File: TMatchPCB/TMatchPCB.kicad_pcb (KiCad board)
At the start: 2 copper layers, 100 x 100 mm, 26 parts, among them J1 CapPlate, J2 CapPlate, J3 BNC, J4 CapPlate, J5 CapPlate, J6 BNC, SW1 SW_SPST, SW2 SW_SPST, SW3 SW_SPST, SW4 SW_SPST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

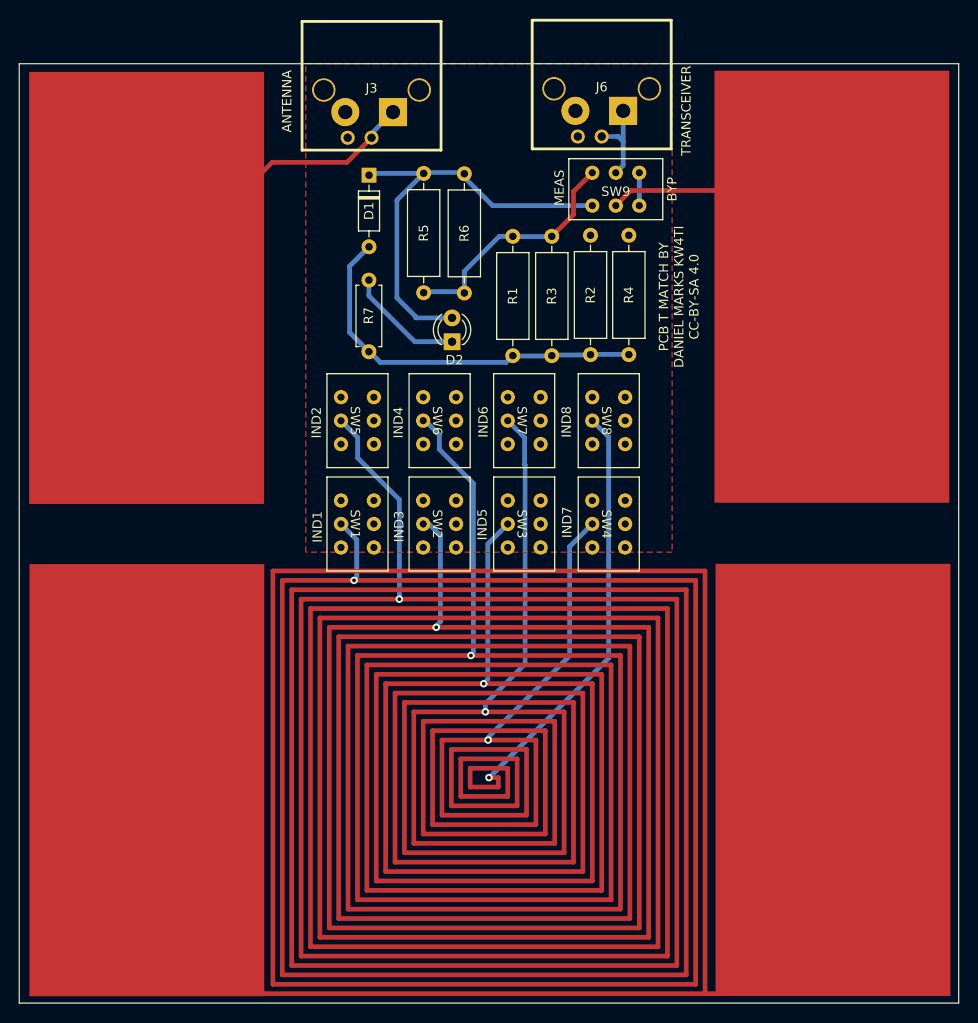
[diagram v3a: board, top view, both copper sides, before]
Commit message: Added 2 more taps for inductor
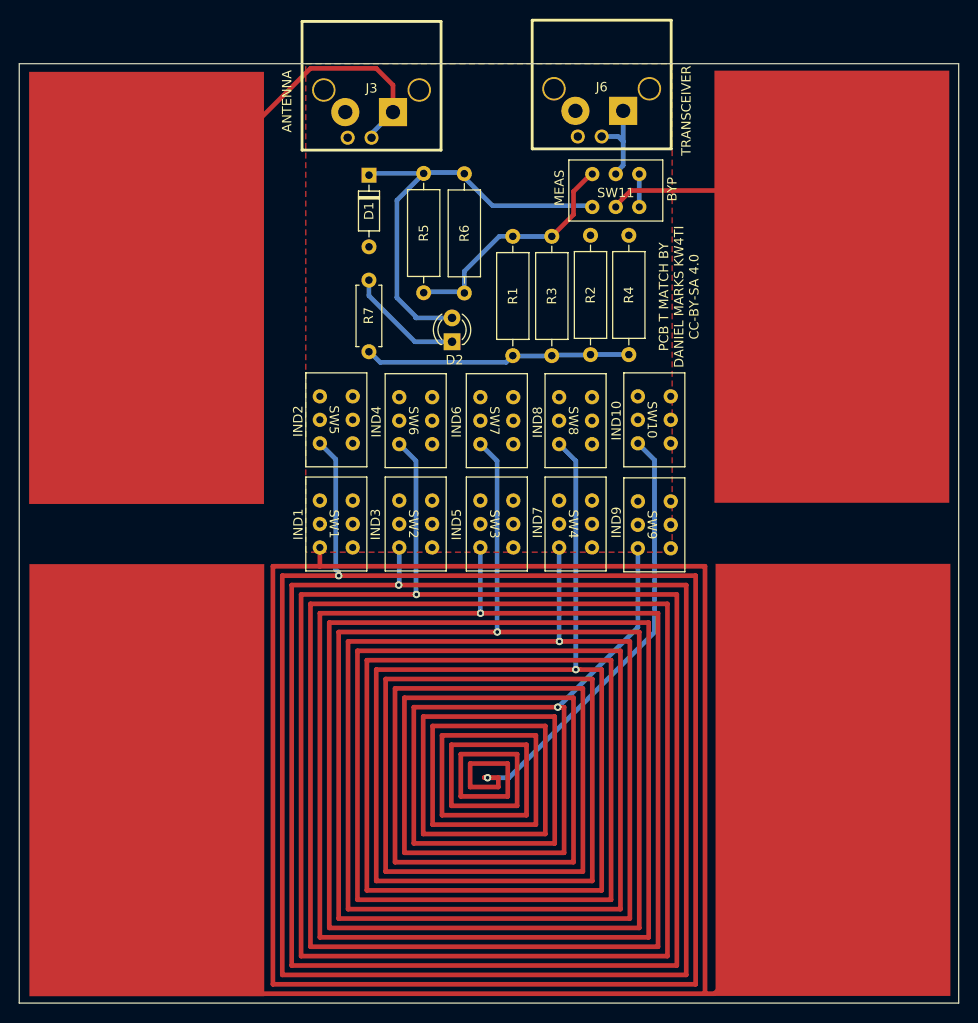
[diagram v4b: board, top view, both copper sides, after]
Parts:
- added SW10: SPST23, TMatchPCB:SS22, F.Cu at (85.9, 57.9)
- added SW11: SW_DPDT_x2, TMatchPCB:SS22, F.Cu at (83.5, 35.2)
- SW1, SW2, SW3, SW4, SW5, SW6, SW7, SW8: value SW_SPST -> SPST23
- SW9: value SW_DPDT_x2 -> SPST23
- moved SW9 34.1 mm to (85.9, 69.1), turned to -90 degrees
- moved SW4 3.53 mm to (77.5, 69.0)
- moved SW8 3.53 mm to (77.5, 58.0)
- moved SW3 2.91 mm to (69.1, 69.0)
- moved SW7 2.91 mm to (69.1, 58.0)
- moved SW2 2.55 mm to (60.5, 69.0)
- moved SW6 2.55 mm to (60.5, 58.0)
- moved SW5 2.25 mm to (52.0, 57.9)
- moved SW1 2.25 mm to (52.0, 69.0)
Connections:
- D2 pad 2: Net-(D2-Pad2) -> Net-(D1-Pad1)
- R1 pad 2: Net-(R1-Pad2) -> Net-(D1-Pad2)
- R2 pad 1: Net-(R1-Pad2) -> Net-(D1-Pad2)
- R3 pad 2: Net-(R1-Pad2) -> Net-(D1-Pad2)
- R4 pad 1: Net-(R1-Pad2) -> Net-(D1-Pad2)
- R5 pad 1: Net-(D2-Pad2) -> Net-(D1-Pad1)
- R6 pad 1: Net-(D2-Pad2) -> Net-(D1-Pad1)
- R7 pad 1: Net-(R1-Pad2) -> Net-(D1-Pad2)
- SW1 pad 1: GND -> (no net)
- SW1 pad 2: Net-(J1-Pad1) -> GND
- SW1 pad 3: (no net) -> Net-(J1-Pad1)
- SW2 pad 1: GND -> (no net)
- SW2 pad 2: Net-(J1-Pad1) -> GND
- SW2 pad 3: (no net) -> Net-(J1-Pad1)
- SW3 pad 1: GND -> (no net)
- SW3 pad 2: Net-(J1-Pad1) -> GND
- SW3 pad 3: (no net) -> Net-(J1-Pad1)
- SW4 pad 1: GND -> (no net)
- SW4 pad 2: Net-(J1-Pad1) -> GND
- SW4 pad 3: (no net) -> Net-(J1-Pad1)
- SW5 pad 1: GND -> (no net)
- SW5 pad 2: Net-(J1-Pad1) -> GND
- SW5 pad 3: (no net) -> Net-(J1-Pad1)
- SW6 pad 1: GND -> (no net)
- SW6 pad 2: Net-(J1-Pad1) -> GND
- SW6 pad 3: (no net) -> Net-(J1-Pad1)
- SW7 pad 1: GND -> (no net)
- SW7 pad 2: Net-(J1-Pad1) -> GND
- SW7 pad 3: (no net) -> Net-(J1-Pad1)
- SW8 pad 1: GND -> (no net)
- SW8 pad 2: Net-(J1-Pad1) -> GND
- SW8 pad 3: (no net) -> Net-(J1-Pad1)
- SW9 pad 1: Net-(D2-Pad2) -> (no net)
- SW9 pad 2: Net-(J5-Pad1) -> GND
- SW9 pad 3: Net-(SW9-Pad3) -> Net-(J1-Pad1)
- SW9 pad 4: Net-(R1-Pad1) -> (no net)
- SW9 pad 5: Net-(J6-Pad1) -> (no net)
- SW9 pad 6: Net-(SW9-Pad3) -> (no net)
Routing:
- net Net-(D2-Pad2): track 47.2 -> 0.00 mm
- net Net-(D1-Pad1): track 0.00 -> 46.8 mm
- net Net-(R1-Pad2): track 41.4 -> 0.00 mm
- net Net-(D1-Pad2): track 0.00 -> 28.5 mm
- net Net-(J1-Pad1): track 2432.6 -> 2407.3 mm, vias 8 -> 9
- net Net-(J3-Pad1): track 40.9 -> 46.7 mm
- net Net-(SW9-Pad3): track 3.50 -> 0.00 mm
- net Net-(SW11-Pad3): track 0.00 -> 3.50 mm
- net Net-(J6-Pad1): track 10.3 -> 9.42 mm
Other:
- board text added: "IND10"
- board text added: "IND9"

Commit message: Tightened up board layout
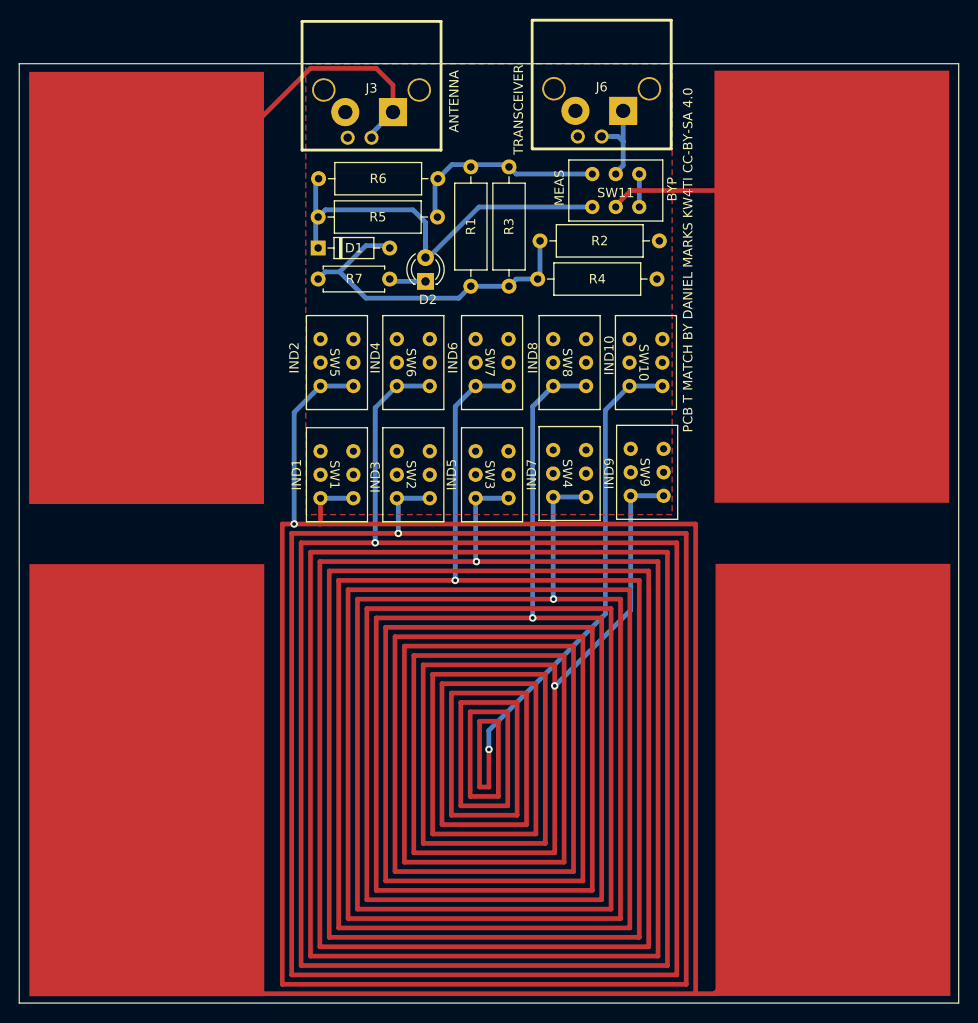
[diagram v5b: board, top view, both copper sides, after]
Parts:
- D1: value 1N5711 -> 1N4148
- SW1, SW10, SW2, SW3, SW4, SW5, SW6, SW7, SW8, SW9: footprint TMatchPCB:SS22 -> TMatchPCB:SS22NB
- moved R6 15.5 mm to (51.9, 32.2), turned to 0 degrees
- moved R2 13.2 mm to (75.4, 38.9), turned to 0 degrees
- moved R4 12.6 mm to (75.2, 42.9), turned to 0 degrees
- moved R5 12.2 mm to (51.8, 36.3), turned to 0 degrees
- moved D1 9.46 mm to (51.8, 39.6), turned to 0 degrees
- moved R7 9.43 mm to (51.8, 42.9), turned to 0 degrees
- moved R3 8.68 mm to (72.1, 31.0)
- moved R1 8.64 mm to (68.1, 31.0)
- moved D2 7.01 mm to (63.2, 43.2)
- moved SW8 6.22 mm to (76.8, 51.8)
- moved SW7 6.20 mm to (68.6, 51.8)
- moved SW6 6.19 mm to (60.2, 51.8)
- moved SW10 6.16 mm to (85.0, 51.8)
- moved SW5 6.10 mm to (52.1, 51.8)
- moved SW9 5.64 mm to (85.1, 63.5)
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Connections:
- R1 pad 2: Net-(D1-Pad2) -> Net-(R1-Pad2)
- R2 pad 1: Net-(D1-Pad2) -> Net-(R1-Pad2)
- R3 pad 2: Net-(D1-Pad2) -> Net-(R1-Pad2)
- R4 pad 1: Net-(D1-Pad2) -> Net-(R1-Pad2)
- R7 pad 1: Net-(D1-Pad2) -> Net-(R1-Pad2)
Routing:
- net Net-(J1-Pad1): track 2407.3 -> 2561.1 mm
- net Net-(R1-Pad2): track 0.00 -> 36.4 mm
- net Net-(D1-Pad2): track 28.5 -> 0.00 mm
- net Net-(D2-Pad1): track 12.5 -> 3.92 mm
- net Net-(R1-Pad1): track 26.2 -> 22.0 mm
- net Net-(D2-Pad2): track 46.8 -> 43.9 mm

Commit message: Picture of assembled T Match
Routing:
- net Net-(J1-Pad1): track 2561.1 -> 2562.1 mm
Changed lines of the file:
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@@
   (segment (start 57.89 71) (end 50 71) (width 0.5) (layer "F.Cu") (net 10))
   (segment (start 52 69) (end 52.07 68.93) (width 0.5) (layer "F.Cu") (net 10))
-  (segment (start 81 80) (end 59 80) (width 0.5) (layer "F.Cu") (net 10))
   (segment (start 65 101) (end 74 101) (width 0.5) (layer "F.Cu") (net 10))
   (segment (start 106.62 106.38) (end 106.62 96.24) (width 0.5) (layer "F.Cu") (net 10))
@@
   (segment (start 76.87 77) (end 56 77) (width 0.5) (layer "F.Cu") (net 10))
   (segment (start 52.07 68.93) (end 52.07 66.254) (width 0.5) (layer "F.Cu") (net 10))
+  (segment (start 74.64 80) (end 59 80) (width 0.5) (layer "F.Cu") (net 10))
   (segment (start 69 97) (end 70 97) (width 0.5) (layer "F.Cu") (net 10))
   (segment (start 60.35 70) (end 49 70) (width 0.5) (layer "F.Cu") (net 10))
@@
   (segment (start 49.26 69) (end 48 69) (width 0.5) (layer "F.Cu") (net 10))
   (segment (start 51 115) (end 88 115) (width 0.5) (layer "F.Cu") (net 10))
+  (segment (start 81 80) (end 74.64 80) (width 0.5) (layer "F.Cu") (net 10))
   (segment (start 78 83) (end 62 83) (width 0.5) (layer "F.Cu") (net 10))
   (segment (start 69 90) (end 69 97) (width 0.5) (layer "F.Cu") (net 10))
@@
   (via (at 49.26 69) (size 0.8) (drill 0.4) (layers "F.Cu" "B.Cu") (net 10))
   (via (at 66.41 75) (size 0.8) (drill 0.4) (layers "F.Cu" "B.Cu") (net 10))
-  (via (at 74.65 79) (size 0.8) (drill 0.4) (layers "F.Cu" "B.Cu") (net 10))
+  (via (at 74.64 80) (size 0.8) (drill 0.4) (layers "F.Cu" "B.Cu") (net 10))
   (via (at 68.67 73) (size 0.8) (drill 0.4) (layers "F.Cu" "B.Cu") (net 10))
   (via (at 57.89 71) (size 0.8) (drill 0.4) (layers "F.Cu" "B.Cu") (net 10))
@@
   (segment (start 82.4 78.57) (end 82.4 56.879) (width 0.5) (layer "B.Cu") (net 10))
   (segment (start 76.87 77) (end 76.835 76.965) (width 0.5) (layer "B.Cu") (net 10))
+  (segment (start 76.835 54.316) (end 74.65 56.501) (width 0.5) (layer "B.Cu") (net 10))
   (segment (start 68.67 73) (end 68.58 72.91) (width 0.5) (layer "B.Cu") (net 10))
   (segment (start 57.89 71) (end 57.89 56.624) (width 0.5) (layer "B.Cu") (net 10))
   (segment (start 72.588 66.254) (end 69.088 66.254) (width 0.5) (layer "B.Cu") (net 10))
-  (segment (start 74.65 56.501) (end 76.835 54.316) (width 0.5) (layer "B.Cu") (net 10))
-  (segment (start 74.65 79) (end 74.65 56.501) (width 0.5) (layer "B.Cu") (net 10))
+  (segment (start 74.65 79.99) (end 74.64 80) (width 0.5) (layer "B.Cu") (net 10))
   (segment (start 57.89 56.624) (end 60.198 54.316) (width 0.5) (layer "B.Cu") (net 10))
   (segment (start 80.335 54.316) (end 76.835 54.316) (width 0.5) (layer "B.Cu") (net 10))
@@
   (segment (start 88.59 66) (end 85.09 66) (width 0.5) (layer "B.Cu") (net 10))
   (segment (start 80.335 66.127) (end 76.835 66.127) (width 0.5) (layer "B.Cu") (net 10))
+  (segment (start 74.65 56.501) (end 74.65 79.99) (width 0.5) (layer "B.Cu") (net 10))
   (segment (start 55.57 54.316) (end 52.07 54.316) (width 0.5) (layer "B.Cu") (net 10))
   (segment (start 66.41 75) (end 66.41 56.486) (width 0.5) (layer "B.Cu") (net 10))

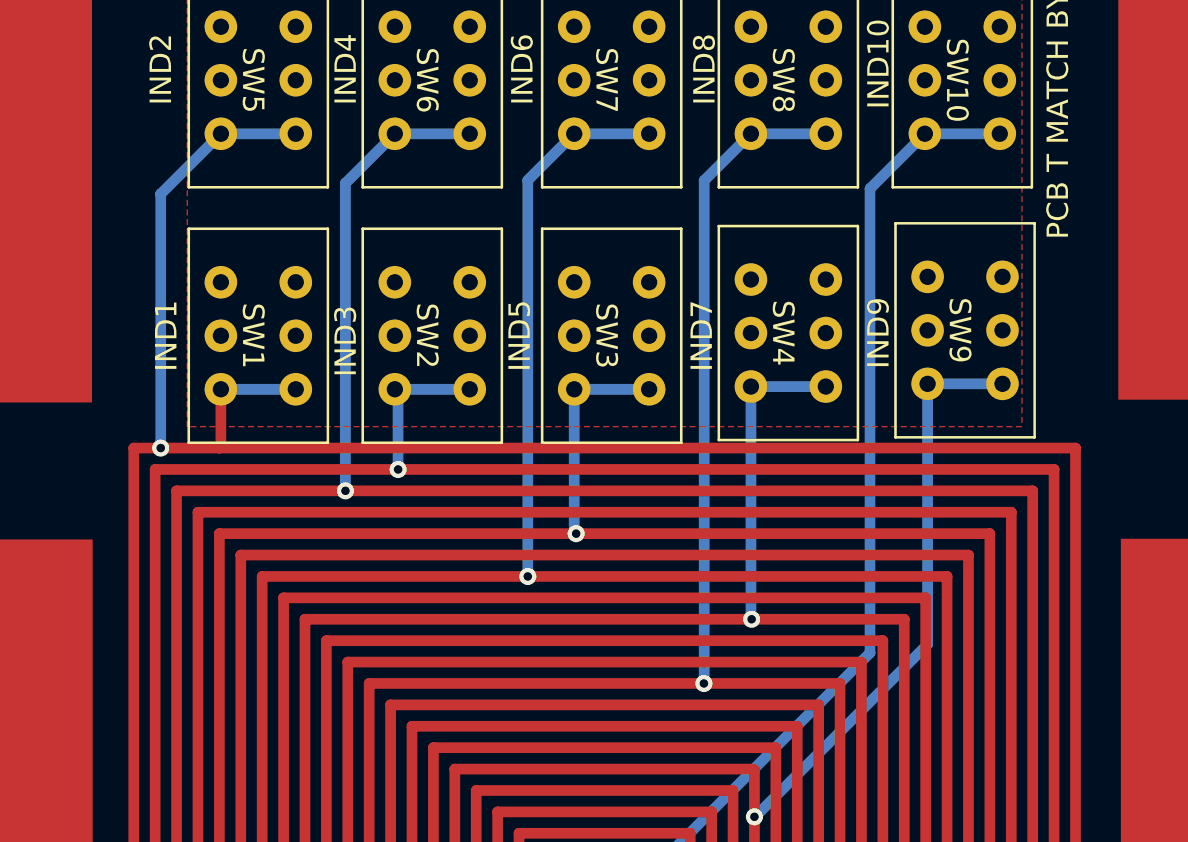
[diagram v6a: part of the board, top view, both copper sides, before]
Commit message: Fixed taps
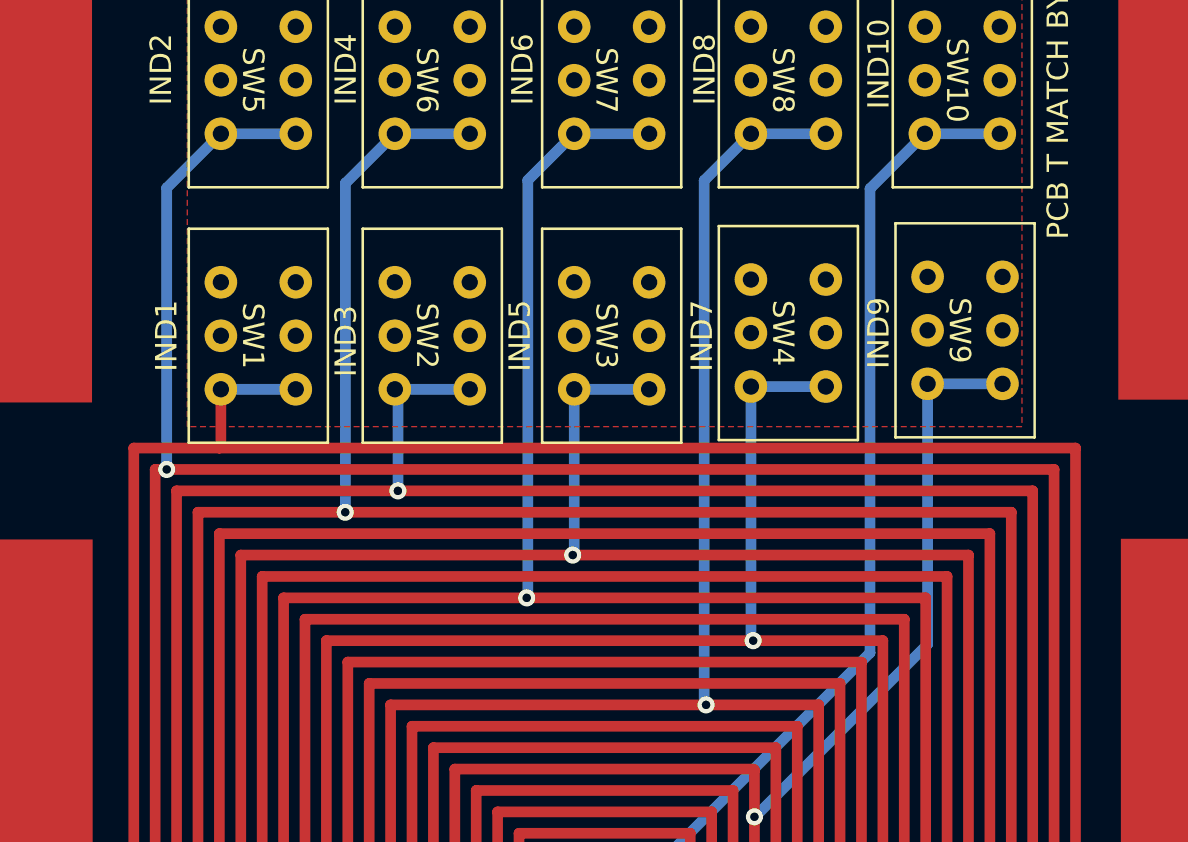
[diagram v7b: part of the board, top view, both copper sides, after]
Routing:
- net Net-(J1-Pad1): track 2562.1 -> 2569.1 mm

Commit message: Added silkscreen instructions and one slide plate
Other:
- board text added: "ANTENNA SIDE"
- board text added: "OFF"
- board text added: "ON"
- board text added: "TRANSMITTER SIDE"
- board text added: "The rough guide to tuning a T-match. - Switch the tuner bridge from BYP to MEAS. - Set the transmitter for low power (less than 5 W) in case the transmitter is capable than more than this power. - Set the capacitor plates on the antenna side for maximum overlap and those on the transmit side for half overlap. - Switching ON only one inductor switch at a time, find the position which dims the LED 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"
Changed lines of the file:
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@@
     (property "Sheetname" "")
     (attr through_hole)
-    (fp_text reference "D2" (at -1.945 0.26) (layer "F.SilkS")
+    (fp_text reference "D2" (at 4.31 -0.036) (layer "F.SilkS")
       (effects (font (size 1 1) (thickness 0.15)))
     )
@@
     (effects (font (size 1 1) (thickness 0.15)) (justify mirror))
   )
+  (gr_text "The rough guide to tuning a T-match.\n\n- Switch the tuner bridge from BYP to MEAS. \n- Set the transmitter for low power (less than 5 W)\n  in case the transmitter is capable than more than\n  this power.\n- Set the capacitor plates on the antenna side for \n  maximum overlap and those on the transmit side\n  for half overlap.\n- Switching ON only one inductor switch at a time,\n  find the position which dims the LED the most.\n- Slide and retighten the capacitor on the transmitter\n  side to dim the LED.\n- Test the other inductor settings to see if the LED\n  can be further dimmed (antenna better matched).\n- Alternate between the transmitter capacitor and \n  inductor to minimize the LED brightness.\n- After tuning the input capacitor and inductor switch,\n  adjust the antenna side capacitor for minimum \n  brightness.  Once you have done this, repeat \n  returning the transmit side capacitor and inductor.\n  The goal is to maximize the antenna side capacitance\n  while achieving a good match with the transmit side\n  capacitor and inductor tap.\n- Record which inductor tap is switched and the \n  position of the plates as indicated by the ruled \n  line position on the edge of the tuner plate for \n  the transmit and antenna side capacitors.\n- Switch the tuner bridge from MEAS to BYP before\n  transmitting.\n" (at 91.5 95) (layer "B.SilkS")
+    (effects (font (size 1 1) (thickness 0.15)) (justify left mirror))
+  )
   (gr_text "4" (at 29 119) (layer "B.SilkS")
     (effects (font (size 1 1) (thickness 0.15)) (justify mirror))
@@
     (effects (font (size 1 1) (thickness 0.15)) (justify mirror))
   )
+  (gr_text "ANTENNA SIDE" (at 48.5 82.5 -90) (layer "B.SilkS")
+    (effects (font (size 1 1) (thickness 0.15)) (justify mirror))
+  )
   (gr_text "10" (at 41 119) (layer "B.SilkS")
     (effects (font (size 1 1) (thickness 0.15)) (justify mirror))
@@
     (effects (font (size 1 1) (thickness 0.15)) (justify mirror))
   )
+  (gr_text "TRANSMITTER SIDE" (at 92.5 83.5 -90) (layer "B.SilkS")
+    (effects (font (size 1 1) (thickness 0.15)) (justify mirror))
+  )
   (gr_text "7" (at 105 21) (layer "B.SilkS")
     (effects (font (size 1 1) (thickness 0.15)) (justify mirror))
@@
     (effects (font (size 1 1) (thickness 0.15)))
   )
+  (gr_text "ON" (at 70.33 69.5) (layer "F.SilkS")
+    (effects (font (size 1 1) (thickness 0.15)))
+  )
   (gr_text "BYP" (at 89.5 33.36 90) (layer "F.SilkS")
     (effects (font (size 1 1) (thickness 0.15)))
@@
     (effects (font (size 1 1) (thickness 0.15)))
   )
+  (gr_text "ON" (at 61.948 69.5) (layer "F.SilkS")
+    (effects (font (size 1 1) (thickness 0.15)))
+  )
   (gr_text "IND2" (at 49.276 51.308 90) (layer "F.SilkS")
     (effects (font (size 1 1) (thickness 0.15)))
   )
+  (gr_text "ON" (at 87 69.5) (layer "F.SilkS")
+    (effects (font (size 1 1) (thickness 0.15)))
+  )
   (gr_text "IND5" (at 66.04 63.754 90) (layer "F.SilkS")
     (effects (font (size 1 1) (thickness 0.15)))
   )
+  (gr_text "ON" (at 53.82 69.5) (layer "F.SilkS")
+    (effects (font (size 1 1) (thickness 0.15)))
+  )
   (gr_text "IND9\n" (at 82.804 63.627 90) (layer "F.SilkS")
     (effects (font (size 1 1) (thickness 0.15)))
@@
     (effects (font (size 1 1) (thickness 0.15)))
   )
+  (gr_text "OFF" (at 53.5 46) (layer "F.SilkS")
+    (effects (font (size 1 1) (thickness 0.15)))
+  )
   (gr_text "IND4" (at 57.912 51.308 90) (layer "F.SilkS")
     (effects (font (size 1 1) (thickness 0.15)))
@@
     (effects (font (size 1 1) (thickness 0.15)))
   )
+  (gr_text "OFF" (at 86.5 46) (layer "F.SilkS")
+    (effects (font (size 1 1) (thickness 0.15)))
+  )
+  (gr_text "OFF" (at 62 46) (layer "F.SilkS")
+    (effects (font (size 1 1) (thickness 0.15)))
+  )
+  (gr_text "OFF" (at 78.5 46) (layer "F.SilkS")
+    (effects (font (size 1 1) (thickness 0.15)))
+  )
   (gr_text "IND6" (at 66.167 51.308 90) (layer "F.SilkS")
     (effects (font (size 1 1) (thickness 0.15)))
   )
+  (gr_text "ON" (at 78.585 69.5) (layer "F.SilkS")
+    (effects (font (size 1 1) (thickness 0.15)))
+  )
   (gr_text "IND1" (at 49.53 63.754 90) (layer "F.SilkS")
     (effects (font (size 1 1) (thickness 0.15)))
@@
     (effects (font (size 1 1) (thickness 0.15)))
   )
+  (gr_text "OFF" (at 70.5 46) (layer "F.SilkS")
+    (effects (font (size 1 1) (thickness 0.15)))
+  )
